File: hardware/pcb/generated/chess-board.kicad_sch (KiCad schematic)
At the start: 303 parts, among them J1 PPPC202LFBN-RC, J2 PPPC041LFBN-RC, J3 PJ-102A, SW1 TL1105SPF100QG, SW10 TL1105SPF100QG, SW11 TL1105SPF100QG, SW12 TL1105SPF100QG, SW13 RA11131100, SW2 TL1105SPF100QG, SW3 TL1105SPF100QG, SW4 TL1105SPF100QG, SW5 TL1105SPF100QG, SW6 TL1105SPF100QG, SW7 TL1105SPF100QG, SW8 TL1105SPF100QG, SW9 TL1105SPF100QG, U1 TCA9554DWR, U10 SK9822-EC20, U11 SK9822-EC20, U12 SK9822-EC20, U13 SK9822-EC20, U14 SK9822-EC20, U15 SK9822-EC20, U16 SK9822-EC20, U17 SK9822-EC20, U18 SK9822-EC20, U19 SK9822-EC20, U2 TCA9554DWR, U20 SK9822-EC20, U21 SK9822-EC20, U22 SK9822-EC20, U23 SK9822-EC20, U24 SK9822-EC20, U25 SK9822-EC20, U26 SK9822-EC20, U27 SK9822-EC20, U28 SK9822-EC20, U29 SK9822-EC20, U3 TCA9554DWR, U30 SK9822-EC20, U31 SK9822-EC20, U32 SK9822-EC20, U33 SK9822-EC20, U34 SK9822-EC20, U35 SK9822-EC20, U36 SK9822-EC20, U37 SK9822-EC20, U38 SK9822-EC20, U39 SK9822-EC20, U4 TCA9554DWR, U40 SK9822-EC20, U41 SK9822-EC20, U42 SK9822-EC20, U43 SK9822-EC20, U44 SK9822-EC20, U45 SK9822-EC20, U46 SK9822-EC20, U47 SK9822-EC20, U48 SK9822-EC20, U49 SK9822-EC20, U5 SN74AHCT125DR, U50 SK9822-EC20, U51 SK9822-EC20, U52 SK9822-EC20, U53 SK9822-EC20, U54 SK9822-EC20, U55 SK9822-EC20, U56 SK9822-EC20, U57 SK9822-EC20, U58 SK9822-EC20, U59 SK9822-EC20, U6 SK9822-EC20, U60 SK9822-EC20, U61 SK9822-EC20, U62 SK9822-EC20, U63 SK9822-EC20, U64 SK9822-EC20, U65 SK9822-EC20, U66 SK9822-EC20, U67 SK9822-EC20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

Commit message: Simplify PCB design pipeline
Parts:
- removed C1: 10ZLJ1000M10X16, symbol Generated:C1
- removed C10: CC0603KRX7R9BB104, symbol Generated:C10
- removed C100: CC0603KRX7R9BB104, symbol Generated:C100
- removed C101: CC0603KRX7R9BB104, symbol Generated:C101
- removed C102: CC0603KRX7R9BB104, symbol Generated:C102
- removed C103: CC0603KRX7R9BB104, symbol Generated:C103
- removed C104: CC0603KRX7R9BB104, symbol Generated:C104
- removed C105: CC0603KRX7R9BB104, symbol Generated:C105
- removed C106: CC0603KRX7R9BB104, symbol Generated:C106
- removed C107: CC0603KRX7R9BB104, symbol Generated:C107
- removed C108: CC0603KRX7R9BB104, symbol Generated:C108
- removed C109: CC0603KRX7R9BB104, symbol Generated:C109
- removed C11: CC0603KRX7R9BB104, symbol Generated:C11
- removed C110: CC0603KRX7R9BB104, symbol Generated:C110
- removed C111: CC0603KRX7R9BB104, symbol Generated:C111
- removed C112: CC0603KRX7R9BB104, symbol Generated:C112
- removed C113: CC0603KRX7R9BB104, symbol Generated:C113
- removed C114: CC0603KRX7R9BB104, symbol Generated:C114
- removed C115: CC0603KRX7R9BB104, symbol Generated:C115
- removed C116: CC0603KRX7R9BB104, symbol Generated:C116
- removed C117: CC0603KRX7R9BB104, symbol Generated:C117
- removed C118: CC0603KRX7R9BB104, symbol Generated:C118
- removed C119: CC0603KRX7R9BB104, symbol Generated:C119
- removed C12: CC0603KRX7R9BB104, symbol Generated:C12
- removed C120: CC0603KRX7R9BB104, symbol Generated:C120
- removed C121: CC0603KRX7R9BB104, symbol Generated:C121
- removed C122: CC0603KRX7R9BB104, symbol Generated:C122
- removed C123: CC0603KRX7R9BB104, symbol Generated:C123
- removed C124: CC0603KRX7R9BB104, symbol Generated:C124
- removed C125: CC0603KRX7R9BB104, symbol Generated:C125
- removed C126: CC0603KRX7R9BB104, symbol Generated:C126
- removed C127: CC0603KRX7R9BB104, symbol Generated:C127
- removed C128: CC0603KRX7R9BB104, symbol Generated:C128
- removed C129: CC0603KRX7R9BB104, symbol Generated:C129
- removed C13: CC0603KRX7R9BB104, symbol Generated:C13
- removed C130: CC0603KRX7R9BB104, symbol Generated:C130
- removed C131: CC0603KRX7R9BB104, symbol Generated:C131
- removed C132: CC0603KRX7R9BB104, symbol Generated:C132
- removed C133: CC0603KRX7R9BB104, symbol Generated:C133
- removed C134: CC0603KRX7R9BB104, symbol Generated:C134
- removed C135: CC0603KRX7R9BB104, symbol Generated:C135
- removed C136: CC0603KRX7R9BB104, symbol Generated:C136
- removed C137: CC0603KRX7R9BB104, symbol Generated:C137
- removed C138: CC0603KRX7R9BB104, symbol Generated:C138
- removed C139: CC0603KRX7R9BB104, symbol Generated:C139
- removed C14: CC0603KRX7R9BB104, symbol Generated:C14
- removed C15: CC0603KRX7R9BB104, symbol Generated:C15
- removed C16: CC0603KRX7R9BB104, symbol Generated:C16
- removed C17: CC0603KRX7R9BB104, symbol Generated:C17
- removed C18: CC0603KRX7R9BB104, symbol Generated:C18
- removed C19: CC0603KRX7R9BB104, symbol Generated:C19
- removed C2: CC0805KKX5R6BB106, symbol Generated:C2
- removed C20: CC0603KRX7R9BB104, symbol Generated:C20
- removed C21: CC0603KRX7R9BB104, symbol Generated:C21
- removed C22: CC0603KRX7R9BB104, symbol Generated:C22
- removed C23: CC0603KRX7R9BB104, symbol Generated:C23
- removed C24: CC0603KRX7R9BB104, symbol Generated:C24
- removed C25: CC0603KRX7R9BB104, symbol Generated:C25
- removed C26: CC0603KRX7R9BB104, symbol Generated:C26
- removed C27: CC0603KRX7R9BB104, symbol Generated:C27
- removed C28: CC0603KRX7R9BB104, symbol Generated:C28
- removed C29: CC0603KRX7R9BB104, symbol Generated:C29
- removed C3: CC0603KRX7R9BB104, symbol Generated:C3
- removed C30: CC0603KRX7R9BB104, symbol Generated:C30
- removed C31: CC0603KRX7R9BB104, symbol Generated:C31
- removed C32: CC0603KRX7R9BB104, symbol Generated:C32
- removed C33: CC0603KRX7R9BB104, symbol Generated:C33
- removed C34: CC0603KRX7R9BB104, symbol Generated:C34
- removed C35: CC0603KRX7R9BB104, symbol Generated:C35
- removed C36: CC0603KRX7R9BB104, symbol Generated:C36
- removed C37: CC0603KRX7R9BB104, symbol Generated:C37
- removed C38: CC0603KRX7R9BB104, symbol Generated:C38
- removed C39: CC0603KRX7R9BB104, symbol Generated:C39
- removed C4: CC0603KRX7R9BB104, symbol Generated:C4
- removed C40: CC0603KRX7R9BB104, symbol Generated:C40
- removed C41: CC0603KRX7R9BB104, symbol Generated:C41
- removed C42: CC0603KRX7R9BB104, symbol Generated:C42
- removed C43: CC0603KRX7R9BB104, symbol Generated:C43
- removed C44: CC0603KRX7R9BB104, symbol Generated:C44
- removed C45: CC0603KRX7R9BB104, symbol Generated:C45
- removed C46: CC0603KRX7R9BB104, symbol Generated:C46
- removed C47: CC0603KRX7R9BB104, symbol Generated:C47
- removed C48: CC0603KRX7R9BB104, symbol Generated:C48
- removed C49: CC0603KRX7R9BB104, symbol Generated:C49
- removed C5: CC0603KRX7R9BB104, symbol Generated:C5
- removed C50: CC0603KRX7R9BB104, symbol Generated:C50
- removed C51: CC0603KRX7R9BB104, symbol Generated:C51
- removed C52: CC0603KRX7R9BB104, symbol Generated:C52
- removed C53: CC0603KRX7R9BB104, symbol Generated:C53
- removed C54: CC0603KRX7R9BB104, symbol Generated:C54
- removed C55: CC0603KRX7R9BB104, symbol Generated:C55
- removed C56: CC0603KRX7R9BB104, symbol Generated:C56
- removed C57: CC0603KRX7R9BB104, symbol Generated:C57
- removed C58: CC0603KRX7R9BB104, symbol Generated:C58
- removed C59: CC0603KRX7R9BB104, symbol Generated:C59
- removed C6: CC0603KRX7R9BB104, symbol Generated:C6
- removed C60: CC0603KRX7R9BB104, symbol Generated:C60
- removed C61: CC0603KRX7R9BB104, symbol Generated:C61
- removed C62: CC0603KRX7R9BB104, symbol Generated:C62
- removed C63: CC0603KRX7R9BB104, symbol Generated:C63
- removed C64: CC0603KRX7R9BB104, symbol Generated:C64
- removed C65: CC0603KRX7R9BB104, symbol Generated:C65
- removed C66: CC0603KRX7R9BB104, symbol Generated:C66
- removed C67: CC0603KRX7R9BB104, symbol Generated:C67
- removed C68: CC0603KRX7R9BB104, symbol Generated:C68
- removed C69: CC0603KRX7R9BB104, symbol Generated:C69
- removed C7: CC0603KRX7R9BB104, symbol Generated:C7
- removed C70: CC0603KRX7R9BB104, symbol Generated:C70
- removed C71: CC0603KRX7R9BB104, symbol Generated:C71
- removed C72: CC0603KRX7R9BB104, symbol Generated:C72
- removed C73: CC0603KRX7R9BB104, symbol Generated:C73
- removed C74: CC0603KRX7R9BB104, symbol Generated:C74
- removed C75: CC0603KRX7R9BB104, symbol Generated:C75
- removed C76: CC0603KRX7R9BB104, symbol Generated:C76
- removed C77: CC0603KRX7R9BB104, symbol Generated:C77
- removed C78: CC0603KRX7R9BB104, symbol Generated:C78
- removed C79: CC0603KRX7R9BB104, symbol Generated:C79
- removed C8: CC0603KRX7R9BB104, symbol Generated:C8
- removed C80: CC0603KRX7R9BB104, symbol Generated:C80
- removed C81: CC0603KRX7R9BB104, symbol Generated:C81
- removed C82: CC0603KRX7R9BB104, symbol Generated:C82
- removed C83: CC0603KRX7R9BB104, symbol Generated:C83
- removed C84: CC0603KRX7R9BB104, symbol Generated:C84
- removed C85: CC0603KRX7R9BB104, symbol Generated:C85
- removed C86: CC0603KRX7R9BB104, symbol Generated:C86
- removed C87: CC0603KRX7R9BB104, symbol Generated:C87
- removed C88: CC0603KRX7R9BB104, symbol Generated:C88
- removed C89: CC0603KRX7R9BB104, symbol Generated:C89
- removed C9: CC0603KRX7R9BB104, symbol Generated:C9
- removed C90: CC0603KRX7R9BB104, symbol Generated:C90
- removed C91: CC0603KRX7R9BB104, symbol Generated:C91
- removed C92: CC0603KRX7R9BB104, symbol Generated:C92
- removed C93: CC0603KRX7R9BB104, symbol Generated:C93
- removed C94: CC0603KRX7R9BB104, symbol Generated:C94
- removed C95: CC0603KRX7R9BB104, symbol Generated:C95
- removed C96: CC0603KRX7R9BB104, symbol Generated:C96
- removed C97: CC0603KRX7R9BB104, symbol Generated:C97
- removed C98: CC0603KRX7R9BB104, symbol Generated:C98
- removed C99: CC0603KRX7R9BB104, symbol Generated:C99
- removed D1: SMBJ6.0A, symbol Generated:D1
- removed F1: 0453002.MR, symbol Generated:F1
- removed HS1: DRV5032FCDBZR, symbol Generated:HS1
- removed HS10: DRV5032FCDBZR, symbol Generated:HS10
- removed HS11: DRV5032FCDBZR, symbol Generated:HS11
- removed HS12: DRV5032FCDBZR, symbol Generated:HS12
- removed HS13: DRV5032FCDBZR, symbol Generated:HS13
- removed HS14: DRV5032FCDBZR, symbol Generated:HS14
- removed HS15: DRV5032FCDBZR, symbol Generated:HS15
- removed HS16: DRV5032FCDBZR, symbol Generated:HS16
- removed HS17: DRV5032FCDBZR, symbol Generated:HS17
- removed HS18: DRV5032FCDBZR, symbol Generated:HS18
- removed HS19: DRV5032FCDBZR, symbol Generated:HS19
- removed HS2: DRV5032FCDBZR, symbol Generated:HS2
- removed HS20: DRV5032FCDBZR, symbol Generated:HS20
- removed HS21: DRV5032FCDBZR, symbol Generated:HS21
- removed HS22: DRV5032FCDBZR, symbol Generated:HS22
- removed HS23: DRV5032FCDBZR, symbol Generated:HS23
- removed HS24: DRV5032FCDBZR, symbol Generated:HS24
- removed HS25: DRV5032FCDBZR, symbol Generated:HS25
- removed HS26: DRV5032FCDBZR, symbol Generated:HS26
- removed HS27: DRV5032FCDBZR, symbol Generated:HS27
- removed HS28: DRV5032FCDBZR, symbol Generated:HS28
- removed HS29: DRV5032FCDBZR, symbol Generated:HS29
- removed HS3: DRV5032FCDBZR, symbol Generated:HS3
- removed HS30: DRV5032FCDBZR, symbol Generated:HS30
- removed HS31: DRV5032FCDBZR, symbol Generated:HS31
- removed HS32: DRV5032FCDBZR, symbol Generated:HS32
- removed HS33: DRV5032FCDBZR, symbol Generated:HS33
- removed HS34: DRV5032FCDBZR, symbol Generated:HS34
- removed HS35: DRV5032FCDBZR, symbol Generated:HS35
- removed HS36: DRV5032FCDBZR, symbol Generated:HS36
- removed HS37: DRV5032FCDBZR, symbol Generated:HS37
- removed HS38: DRV5032FCDBZR, symbol Generated:HS38
- removed HS39: DRV5032FCDBZR, symbol Generated:HS39
- removed HS4: DRV5032FCDBZR, symbol Generated:HS4
- removed HS40: DRV5032FCDBZR, symbol Generated:HS40
- removed HS41: DRV5032FCDBZR, symbol Generated:HS41
- removed HS42: DRV5032FCDBZR, symbol Generated:HS42
- removed HS43: DRV5032FCDBZR, symbol Generated:HS43
- removed HS44: DRV5032FCDBZR, symbol Generated:HS44
- removed HS45: DRV5032FCDBZR, symbol Generated:HS45
- removed HS46: DRV5032FCDBZR, symbol Generated:HS46
- removed HS47: DRV5032FCDBZR, symbol Generated:HS47
- removed HS48: DRV5032FCDBZR, symbol Generated:HS48
- removed HS49: DRV5032FCDBZR, symbol Generated:HS49
- removed HS5: DRV5032FCDBZR, symbol Generated:HS5
- removed HS50: DRV5032FCDBZR, symbol Generated:HS50
- removed HS51: DRV5032FCDBZR, symbol Generated:HS51
- removed HS52: DRV5032FCDBZR, symbol Generated:HS52
- removed HS53: DRV5032FCDBZR, symbol Generated:HS53
- removed HS54: DRV5032FCDBZR, symbol Generated:HS54
- removed HS55: DRV5032FCDBZR, symbol Generated:HS55
- removed HS56: DRV5032FCDBZR, symbol Generated:HS56
- removed HS57: DRV5032FCDBZR, symbol Generated:HS57
- removed HS58: DRV5032FCDBZR, symbol Generated:HS58
- removed HS59: DRV5032FCDBZR, symbol Generated:HS59
- removed HS6: DRV5032FCDBZR, symbol Generated:HS6
- removed HS60: DRV5032FCDBZR, symbol Generated:HS60
- removed HS61: DRV5032FCDBZR, symbol Generated:HS61
- removed HS62: DRV5032FCDBZR, symbol Generated:HS62
- removed HS63: DRV5032FCDBZR, symbol Generated:HS63
- removed HS64: DRV5032FCDBZR, symbol Generated:HS64
- removed HS7: DRV5032FCDBZR, symbol Generated:HS7
- removed HS8: DRV5032FCDBZR, symbol Generated:HS8
- removed HS9: DRV5032FCDBZR, symbol Generated:HS9
- removed J1: PPPC202LFBN-RC, symbol Generated:J1
- removed J2: PPPC041LFBN-RC, symbol Generated:J2
- removed J3: PJ-102A, symbol Generated:J3
- removed R1: RC0603FR-074K7L, symbol Generated:R1
- removed R2: RC0603FR-074K7L, symbol Generated:R2
- removed SW1: TL1105SPF100QG, symbol Generated:SW1
- removed SW10: TL1105SPF100QG, symbol Generated:SW10
- removed SW11: TL1105SPF100QG, symbol Generated:SW11
- removed SW12: TL1105SPF100QG, symbol Generated:SW12
- removed SW13: RA11131100, symbol Generated:SW13
- removed SW2: TL1105SPF100QG, symbol Generated:SW2
- removed SW3: TL1105SPF100QG, symbol Generated:SW3
- removed SW4: TL1105SPF100QG, symbol Generated:SW4
- removed SW5: TL1105SPF100QG, symbol Generated:SW5
- removed SW6: TL1105SPF100QG, symbol Generated:SW6
- removed SW7: TL1105SPF100QG, symbol Generated:SW7
- removed SW8: TL1105SPF100QG, symbol Generated:SW8
- removed SW9: TL1105SPF100QG, symbol Generated:SW9
- removed TP1: S1751-46R, symbol Generated:TP1
- removed TP2: S1751-46R, symbol Generated:TP2
- removed TP3: S1751-46R, symbol Generated:TP3
- removed TP4: S1751-46R, symbol Generated:TP4
- removed TP5: S1751-46R, symbol Generated:TP5
- removed TP6: S1751-46R, symbol Generated:TP6
- removed TP7: S1751-46R, symbol Generated:TP7
- removed U1: TCA9554DWR, symbol Generated:U1
- removed U10: SK9822-EC20, symbol Generated:U10
- removed U11: SK9822-EC20, symbol Generated:U11
- removed U12: SK9822-EC20, symbol Generated:U12
- removed U13: SK9822-EC20, symbol Generated:U13
- removed U14: SK9822-EC20, symbol Generated:U14
- removed U15: SK9822-EC20, symbol Generated:U15
- removed U16: SK9822-EC20, symbol Generated:U16
- removed U17: SK9822-EC20, symbol Generated:U17
- removed U18: SK9822-EC20, symbol Generated:U18
- removed U19: SK9822-EC20, symbol Generated:U19
- removed U2: TCA9554DWR, symbol Generated:U2
- removed U20: SK9822-EC20, symbol Generated:U20
- removed U21: SK9822-EC20, symbol Generated:U21
- removed U22: SK9822-EC20, symbol Generated:U22
- removed U23: SK9822-EC20, symbol Generated:U23
- removed U24: SK9822-EC20, symbol Generated:U24
- removed U25: SK9822-EC20, symbol Generated:U25
- removed U26: SK9822-EC20, symbol Generated:U26
- removed U27: SK9822-EC20, symbol Generated:U27
- removed U28: SK9822-EC20, symbol Generated:U28
- removed U29: SK9822-EC20, symbol Generated:U29
- removed U3: TCA9554DWR, symbol Generated:U3
- removed U30: SK9822-EC20, symbol Generated:U30
- removed U31: SK9822-EC20, symbol Generated:U31
- removed U32: SK9822-EC20, symbol Generated:U32
- removed U33: SK9822-EC20, symbol Generated:U33
- removed U34: SK9822-EC20, symbol Generated:U34
- removed U35: SK9822-EC20, symbol Generated:U35
- removed U36: SK9822-EC20, symbol Generated:U36
- removed U37: SK9822-EC20, symbol Generated:U37
- removed U38: SK9822-EC20, symbol Generated:U38
- removed U39: SK9822-EC20, symbol Generated:U39
- removed U4: TCA9554DWR, symbol Generated:U4
- removed U40: SK9822-EC20, symbol Generated:U40
- removed U41: SK9822-EC20, symbol Generated:U41
- removed U42: SK9822-EC20, symbol Generated:U42
- removed U43: SK9822-EC20, symbol Generated:U43
- removed U44: SK9822-EC20, symbol Generated:U44
- removed U45: SK9822-EC20, symbol Generated:U45
- removed U46: SK9822-EC20, symbol Generated:U46
- removed U47: SK9822-EC20, symbol Generated:U47
- removed U48: SK9822-EC20, symbol Generated:U48
- removed U49: SK9822-EC20, symbol Generated:U49
- removed U5: SN74AHCT125DR, symbol Generated:U5
- removed U50: SK9822-EC20, symbol Generated:U50
- removed U51: SK9822-EC20, symbol Generated:U51
- removed U52: SK9822-EC20, symbol Generated:U52
- removed U53: SK9822-EC20, symbol Generated:U53
- removed U54: SK9822-EC20, symbol Generated:U54
- removed U55: SK9822-EC20, symbol Generated:U55
- removed U56: SK9822-EC20, symbol Generated:U56
- removed U57: SK9822-EC20, symbol Generated:U57
- removed U58: SK9822-EC20, symbol Generated:U58
- removed U59: SK9822-EC20, symbol Generated:U59
- removed U6: SK9822-EC20, symbol Generated:U6
- removed U60: SK9822-EC20, symbol Generated:U60
- removed U61: SK9822-EC20, symbol Generated:U61
- removed U62: SK9822-EC20, symbol Generated:U62
- removed U63: SK9822-EC20, symbol Generated:U63
- removed U64: SK9822-EC20, symbol Generated:U64
- removed U65: SK9822-EC20, symbol Generated:U65
- removed U66: SK9822-EC20, symbol Generated:U66
- removed U67: SK9822-EC20, symbol Generated:U67
- removed U68: SK9822-EC20, symbol Generated:U68
- removed U69: SK9822-EC20, symbol Generated:U69
- removed U7: SK9822-EC20, symbol Generated:U7
- removed U70: TCA9554DWR, symbol Generated:U70
- removed U71: TCA9554DWR, symbol Generated:U71
- removed U72: TCA9554DWR, symbol Generated:U72
- removed U73: TCA9554DWR, symbol Generated:U73
- removed U8: SK9822-EC20, symbol Generated:U8
- removed U9: SK9822-EC20, symbol Generated:U9
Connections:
- no-connect marks 24 -> 0
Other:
- added sheet bank-A1-D2 (bank-A1-D2.kicad_sch)
- added sheet bank-A3-D4 (bank-A3-D4.kicad_sch)
- added sheet bank-A5-D6 (bank-A5-D6.kicad_sch)
- added sheet bank-A7-D8 (bank-A7-D8.kicad_sch)
- added sheet bank-E1-H2 (bank-E1-H2.kicad_sch)
- added sheet bank-E3-H4 (bank-E3-H4.kicad_sch)
- added sheet bank-E5-H6 (bank-E5-H6.kicad_sch)
- added sheet bank-E7-H8 (bank-E7-H8.kicad_sch)
- added sheet controls (controls.kicad_sch)
- added sheet power (power.kicad_sch)
- company: Chess -> (none)

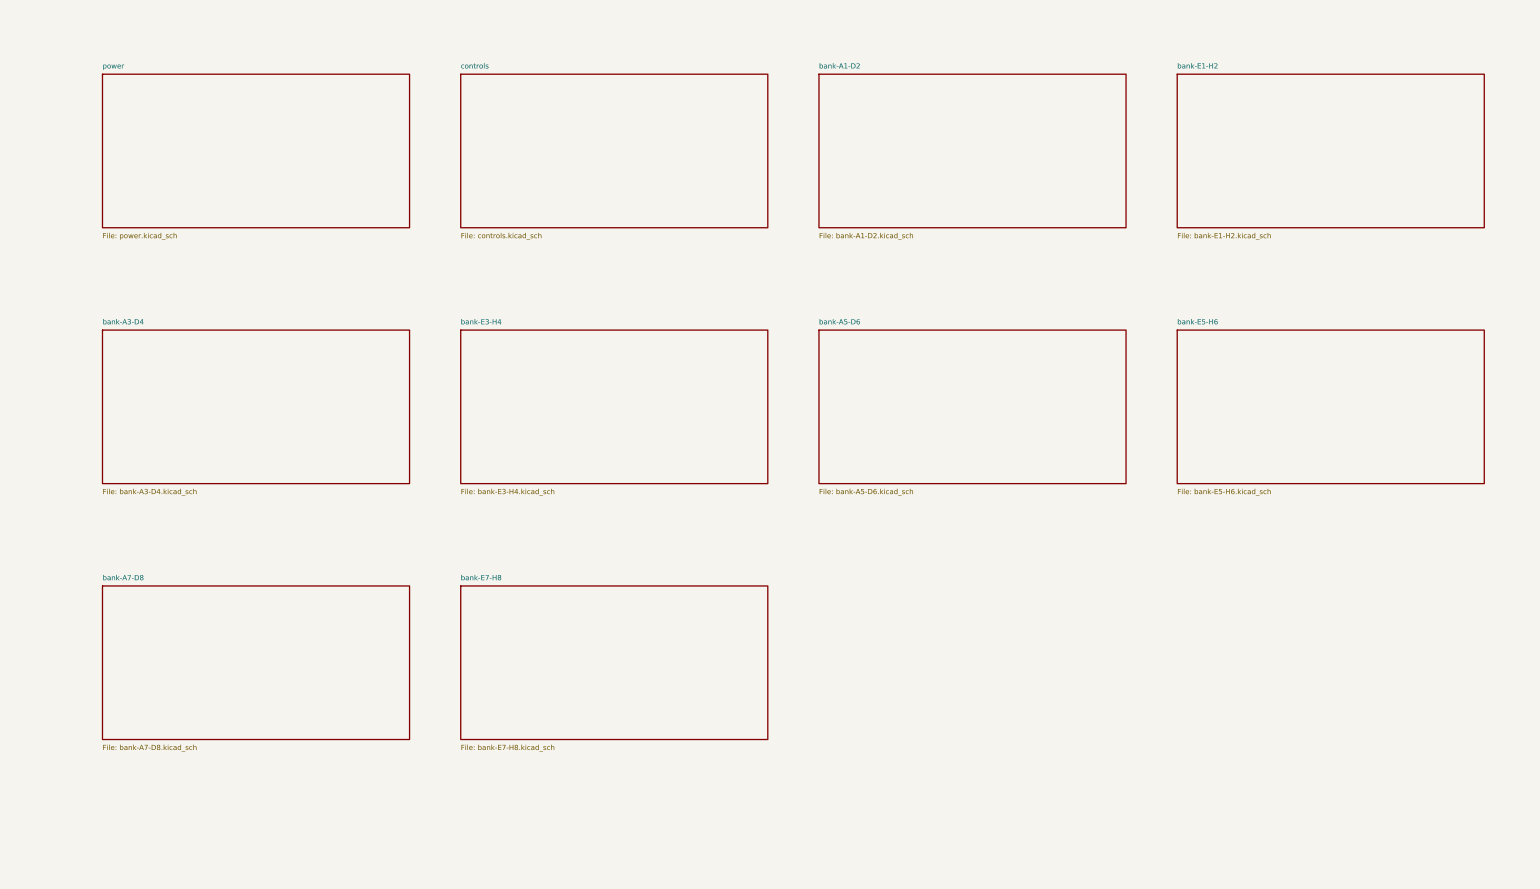
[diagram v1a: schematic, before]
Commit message: build: replace PCB exports with the harness-generated package
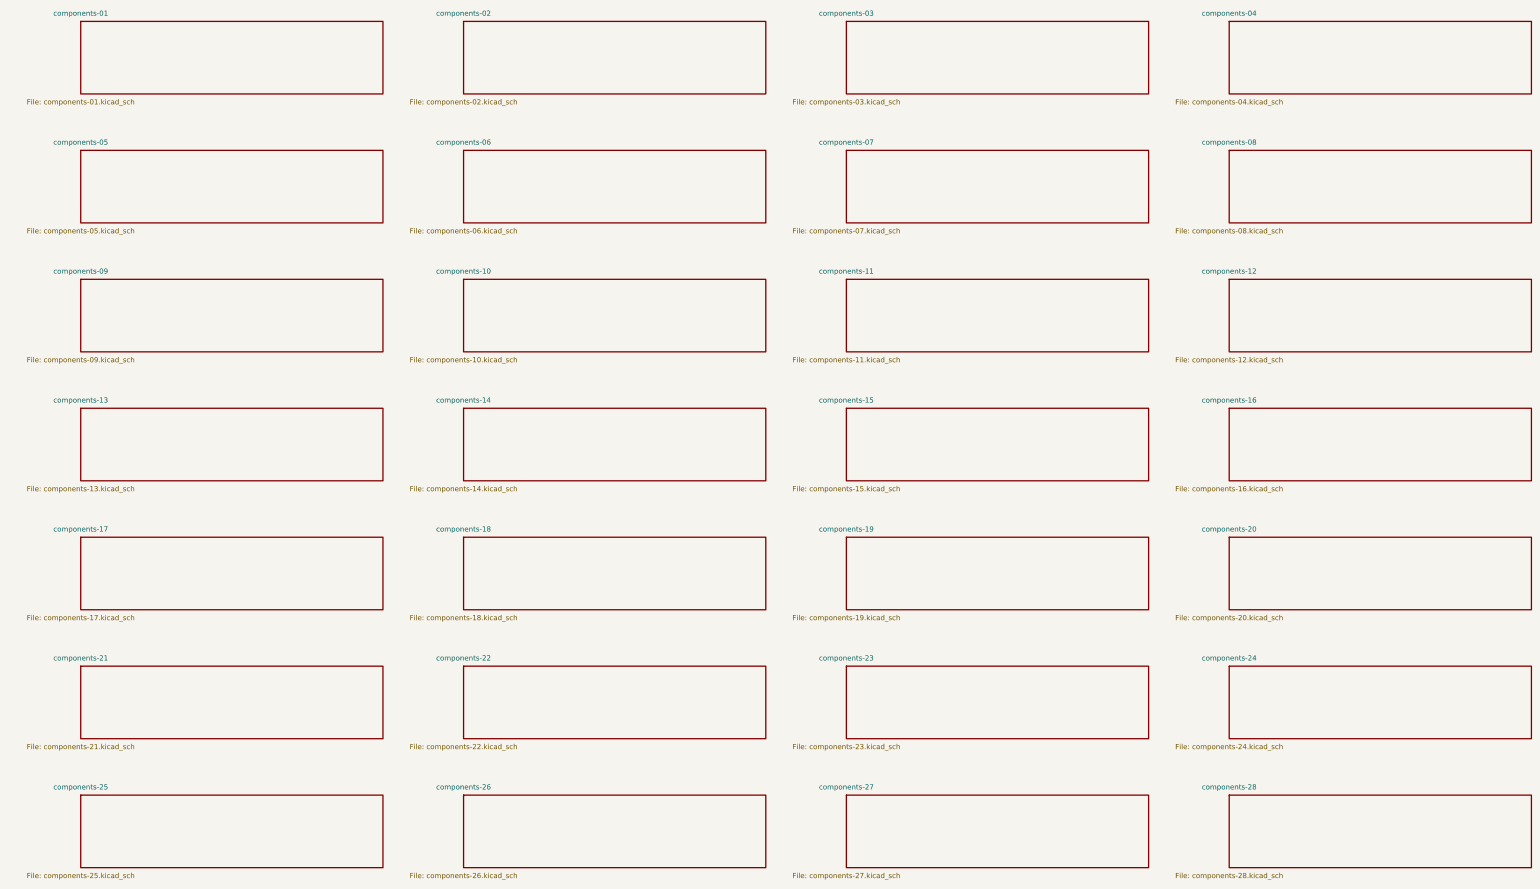
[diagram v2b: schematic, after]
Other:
- removed sheet bank-A1-D2
- removed sheet bank-A3-D4
- removed sheet bank-A5-D6
- removed sheet bank-A7-D8
- removed sheet bank-E1-H2
- removed sheet bank-E3-H4
- removed sheet bank-E5-H6
- removed sheet bank-E7-H8
- removed sheet controls
- removed sheet power
- added sheet components-01 (components-01.kicad_sch)
- added sheet components-02 (components-02.kicad_sch)
- added sheet components-03 (components-03.kicad_sch)
- added sheet components-04 (components-04.kicad_sch)
- added sheet components-05 (components-05.kicad_sch)
- added sheet components-06 (components-06.kicad_sch)
- added sheet components-07 (components-07.kicad_sch)
- added sheet components-08 (components-08.kicad_sch)
- added sheet components-09 (components-09.kicad_sch)
- added sheet components-10 (components-10.kicad_sch)
- added sheet components-11 (components-11.kicad_sch)
- added sheet components-12 (components-12.kicad_sch)
- added sheet components-13 (components-13.kicad_sch)
- added sheet components-14 (components-14.kicad_sch)
- added sheet components-15 (components-15.kicad_sch)
- added sheet components-16 (components-16.kicad_sch)
- added sheet components-17 (components-17.kicad_sch)
- added sheet components-18 (components-18.kicad_sch)
- added sheet components-19 (components-19.kicad_sch)
- added sheet components-20 (components-20.kicad_sch)
- added sheet components-21 (components-21.kicad_sch)
- added sheet components-22 (components-22.kicad_sch)
- added sheet components-23 (components-23.kicad_sch)
- added sheet components-24 (components-24.kicad_sch)
- added sheet components-25 (components-25.kicad_sch)
- added sheet components-26 (components-26.kicad_sch)
- added sheet components-27 (components-27.kicad_sch)
- added sheet components-28 (components-28.kicad_sch)
- title: Chess Smart Board - Single Board Electronics -> Connection index
